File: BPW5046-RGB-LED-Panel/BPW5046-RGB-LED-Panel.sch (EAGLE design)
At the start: 2 parts, among them J1 COCOON_16BIT

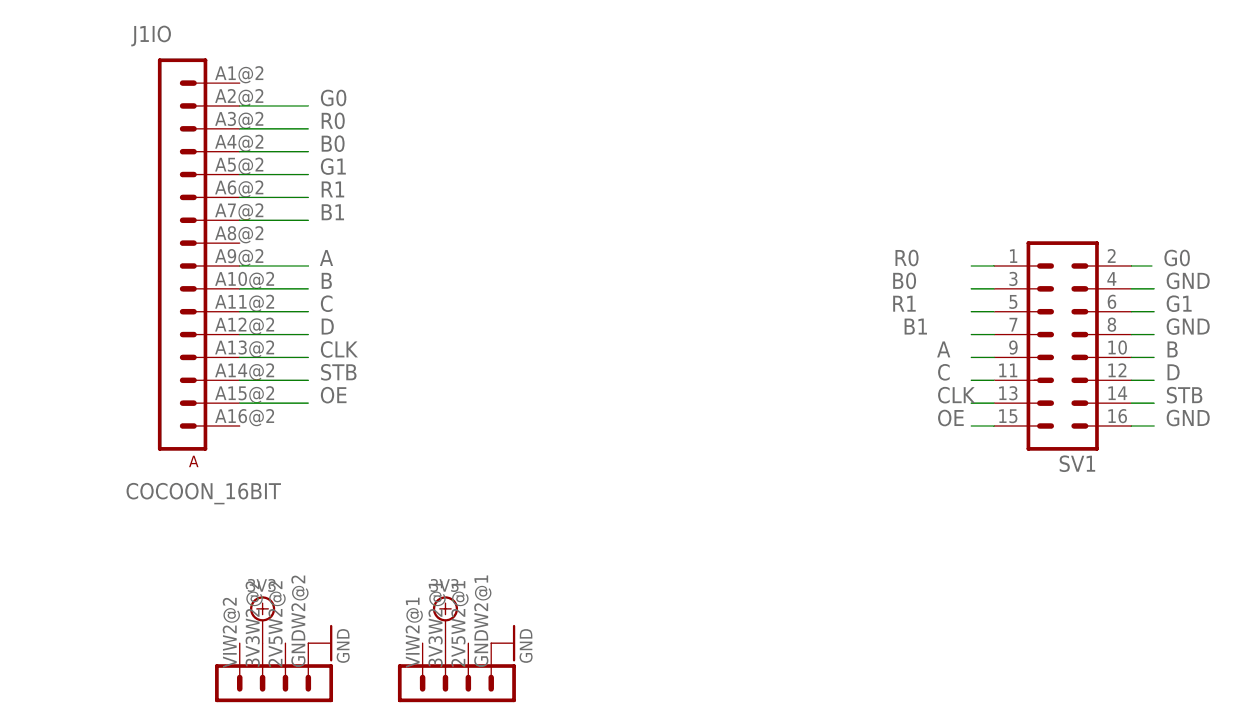
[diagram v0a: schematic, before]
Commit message: RGB LED Panel
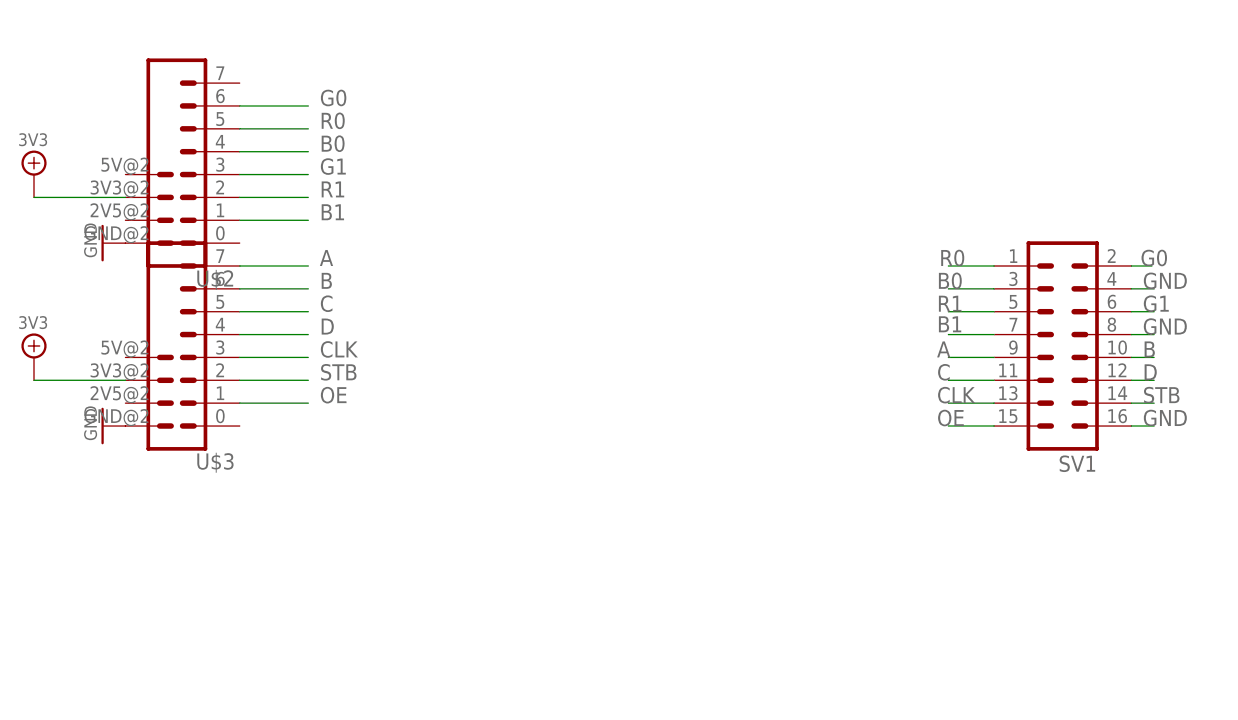
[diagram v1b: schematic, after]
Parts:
- removed J1: COCOON_16BIT, usb1:COCOON_16BIT
- added U$2, U$3: WING8WING8_NOHOLES, Papilio:WING8WING8_NOHOLES
- SV1: PARTNO (none) -> PRPC004DAAN-RC
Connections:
- net 3V3: now also U$2.3V3, U$3.3V3; no longer J1PWRH.3V3, J1PWRL.3V3
- net A: now also U$3.8; no longer J1IO.A9
- net B: now also U$3.7; no longer J1IO.A10
- net B0: now also U$2.5; no longer J1IO.A4
- net B1: now also U$2.2; no longer J1IO.A7
- net C: now also U$3.6; no longer J1IO.A11
- net CLK: now also U$3.4; no longer J1IO.A13
- net D: now also U$3.5; no longer J1IO.A12
- net G0: now also U$2.7; no longer J1IO.A2
- net G1: now also U$2.4; no longer J1IO.A5
- net GND: now also U$2.GND, U$3.GND; no longer J1PWRH.GND, J1PWRL.GND
- net OE: now also U$3.2; no longer J1IO.A15
- net R0: now also U$2.6; no longer J1IO.A3
- net R1: now also U$2.3; no longer J1IO.A6
- net STB: now also U$3.3; no longer J1IO.A14
